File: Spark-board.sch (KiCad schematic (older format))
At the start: 12 parts

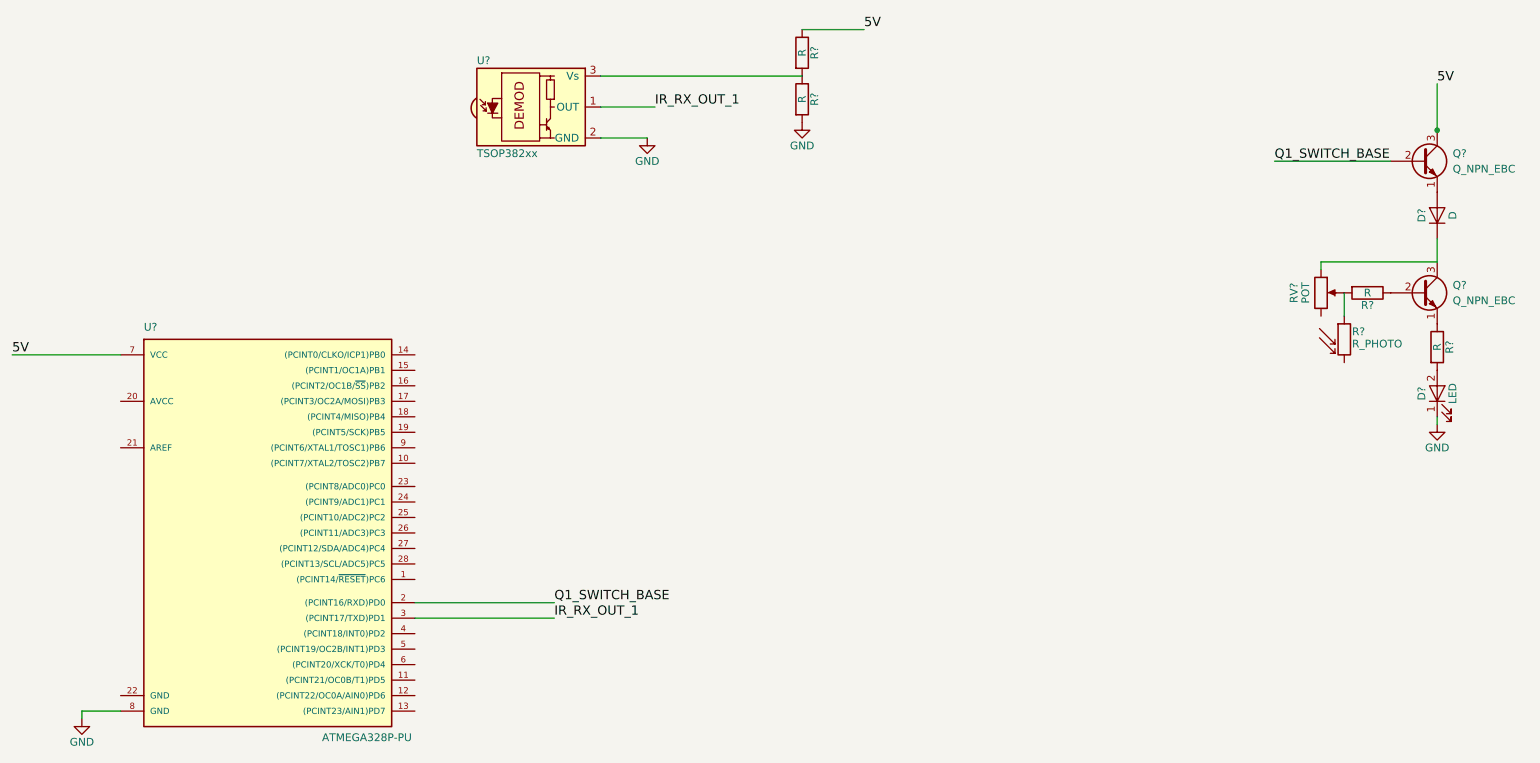
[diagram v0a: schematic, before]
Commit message: - Annotated components
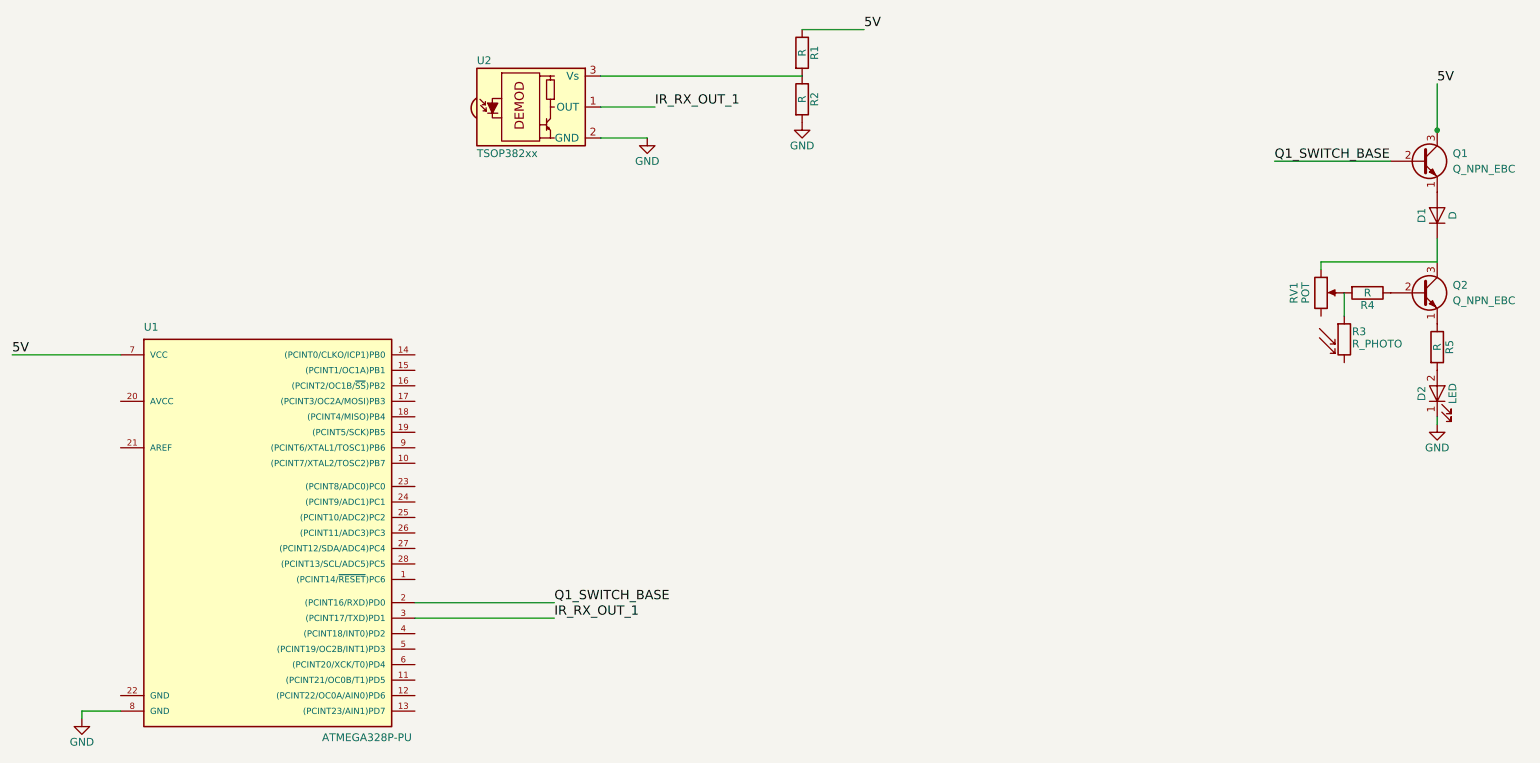
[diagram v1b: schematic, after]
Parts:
- gave numbers to parts that had none: 12
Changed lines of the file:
@@
 $EndDescr
 $Comp
-L POT RV?
+L POT RV1
 U 1 1 5BE8E67D
 P 9250 2400
-F 0 "RV?" V 9075 2400 50  0000 C CNN
+F 0 "RV1" V 9075 2400 50  0000 C CNN
 F 1 "POT" V 9150 2400 50  0000 C CNN
 F 2 "" H 9250 2400 50  0001 C CNN
@@
 $EndComp
 $Comp
-L D D?
+L D D1
 U 1 1 5BE8E73B
 P 10000 1900
-F 0 "D?" H 10000 2000 50  0000 C CNN
+F 0 "D1" H 10000 2000 50  0000 C CNN
 F 1 "D" H 10000 1800 50  0000 C CNN
 F 2 "" H 10000 1900 50  0001 C CNN
@@
 $EndComp
 $Comp
-L Q_NPN_EBC Q?
+L Q_NPN_EBC Q1
 U 1 1 5BE8E792
 P 9900 1550
-F 0 "Q?" H 10100 1600 50  0000 L CNN
+F 0 "Q1" H 10100 1600 50  0000 L CNN
 F 1 "Q_NPN_EBC" H 10100 1500 50  0000 L CNN
 F 2 "" H 10100 1650 50  0001 C CNN
@@
 $EndComp
 $Comp
-L Q_NPN_EBC Q?
+L Q_NPN_EBC Q2
 U 1 1 5BE8E8A3
 P 9900 2400
-F 0 "Q?" H 10100 2450 50  0000 L CNN
+F 0 "Q2" H 10100 2450 50  0000 L CNN
 F 1 "Q_NPN_EBC" H 10100 2350 50  0000 L CNN
 F 2 "" H 10100 2500 50  0001 C CNN
@@
 $EndComp
 $Comp
-L R R?
+L R R4
 U 1 1 5BE8EA00
 P 9550 2400
-F 0 "R?" V 9630 2400 50  0000 C CNN
+F 0 "R4" V 9630 2400 50  0000 C CNN
 F 1 "R" V 9550 2400 50  0000 C CNN
 F 2 "" V 9480 2400 50  0001 C CNN
@@
 	10000 2200 10000 2050
 $Comp
-L R R?
+L R R5
 U 1 1 5BE8EB2A
 P 10000 2750
-F 0 "R?" V 10080 2750 50  0000 C CNN
+F 0 "R5" V 10080 2750 50  0000 C CNN
 F 1 "R" V 10000 2750 50  0000 C CNN
 F 2 "" V 9930 2750 50  0001 C CNN
@@
 $EndComp
 $Comp
-L LED D?
+L LED D2
 U 1 1 5BE8EB6D
 P 10000 3050
-F 0 "D?" H 10000 3150 50  0000 C CNN
+F 0 "D2" H 10000 3150 50  0000 C CNN
 F 1 "LED" H 10000 2950 50  0000 C CNN
 F 2 "" H 10000 3050 50  0001 C CNN
@@
 $EndComp
 $Comp
-L GND #PWR?
+L GND #PWR4
 U 1 1 5BE8EDF4
 P 10000 3250
-F 0 "#PWR?" H 10000 3000 50  0001 C CNN
+F 0 "#PWR4" H 10000 3000 50  0001 C CNN
 F 1 "GND" H 10000 3100 50  0000 C CNN
 F 2 "" H 10000 3250 50  0001 C CNN
@@
 	10000 3200 10000 3250
 $Comp
-L R_PHOTO R?
+L R_PHOTO R3
 U 1 1 5BE8EE4E
 P 9400 2700
-F 0 "R?" H 9450 2750 50  0000 L CNN
+F 0 "R3" H 9450 2750 50  0000 L CNN
 F 1 "R_PHOTO" H 9450 2700 50  0000 L TNN
 F 2 "" V 9450 2450 50  0001 L CNN
@@
 	9400 2550 9400 2400
 $Comp
-L ATMEGA328P-PU U?
+L ATMEGA328P-PU U1
 U 1 1 5BE8F131
 P 2400 3900
-F 0 "U?" H 1650 5150 50  0000 L BNN
+F 0 "U1" H 1650 5150 50  0000 L BNN
 F 1 "ATMEGA328P-PU" H 2800 2500 50  0000 L BNN
 F 2 "DIL28" H 2400 3900 50  0001 C CIN
@@
 Connection ~ 10000 1350
 $Comp
-L GND #PWR?
+L GND #PWR1
 U 1 1 5BEA3ECB
 P 1250 5150
-F 0 "#PWR?" H 1250 4900 50  0001 C CNN
+F 0 "#PWR1" H 1250 4900 50  0001 C CNN
 F 1 "GND" H 1250 5000 50  0000 C CNN
 F 2 "" H 1250 5150 50  0001 C CNN
@@
 5V
 $Comp
-L TSOP382xx U?
+L TSOP382xx U2
 U 1 1 5BF22523
 P 4200 1200
-F 0 "U?" H 3800 1500 50  0000 L CNN
+F 0 "U2" H 3800 1500 50  0000 L CNN
 F 1 "TSOP382xx" H 3800 900 50  0000 L CNN
 F 2 "Opto-Devices:IRReceiver_Vishay_MINICAST-3pin" H 4150 825 50  0001 C CNN
@@
 $EndComp
 $Comp
-L GND #PWR?
+L GND #PWR2
 U 1 1 5BF225DA
 P 4900 1400
-F 0 "#PWR?" H 4900 1150 50  0001 C CNN
+F 0 "#PWR2" H 4900 1150 50  0001 C CNN
 F 1 "GND" H 4900 1250 50  0000 C CNN
 F 2 "" H 4900 1400 50  0001 C CNN
@@
 	4600 1400 4900 1400
 $Comp
-L R R?
+L R R2
 U 1 1 5BF22754
 P 5900 1150
-F 0 "R?" V 5980 1150 50  0000 C CNN
+F 0 "R2" V 5980 1150 50  0000 C CNN
 F 1 "R" V 5900 1150 50  0000 C CNN
 F 2 "" V 5830 1150 50  0001 C CNN
@@
 $EndComp
 $Comp
-L R R?
+L R R1
 U 1 1 5BF227B9
 P 5900 850
-F 0 "R?" V 5980 850 50  0000 C CNN
+F 0 "R1" V 5980 850 50  0000 C CNN
 F 1 "R" V 5900 850 50  0000 C CNN
 F 2 "" V 5830 850 50  0001 C CNN
@@
 5V
 $Comp
-L GND #PWR?
+L GND #PWR3
 U 1 1 5BF22B42
 P 5900 1300
-F 0 "#PWR?" H 5900 1050 50  0001 C CNN
+F 0 "#PWR3" H 5900 1050 50  0001 C CNN
 F 1 "GND" H 5900 1150 50  0000 C CNN
 F 2 "" H 5900 1300 50  0001 C CNN

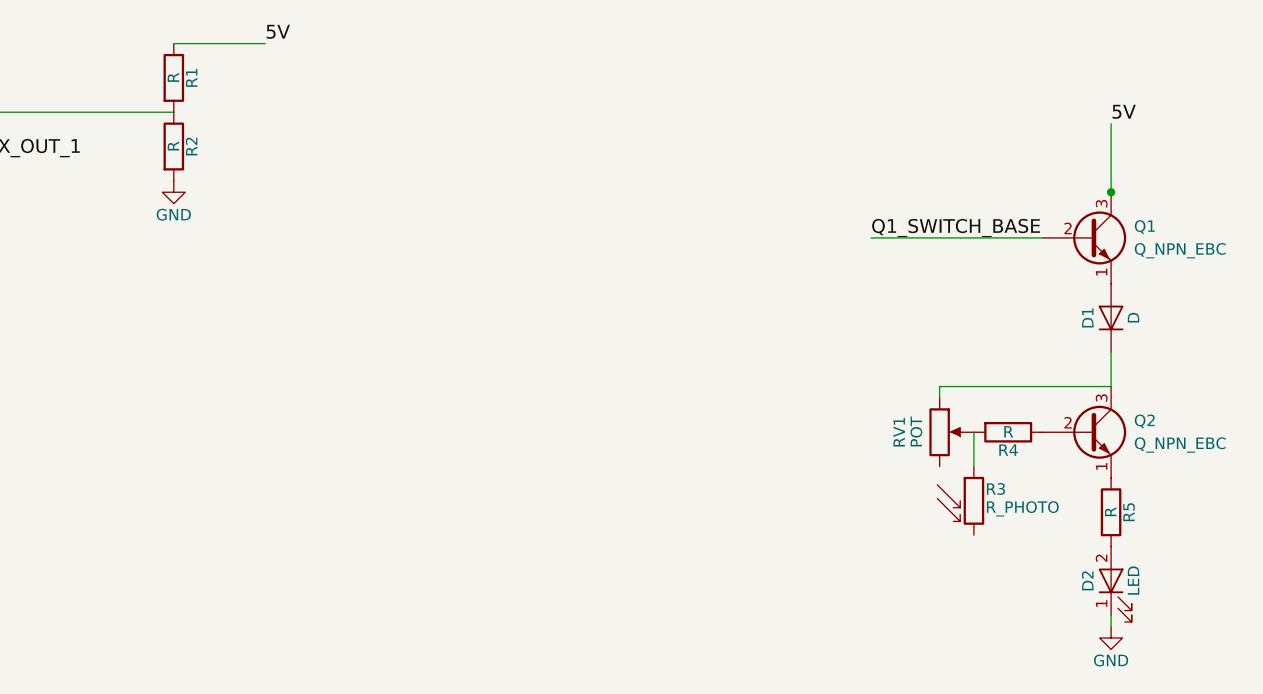
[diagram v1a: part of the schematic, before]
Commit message: - Added values to all resistors
- IR Rx receiver: Voltage divider should provide ~3.3V at Vs input
- Q1 Base: Voltage divider should provide adequate voltage to just keep LED off
           while ensure low current through transistor base
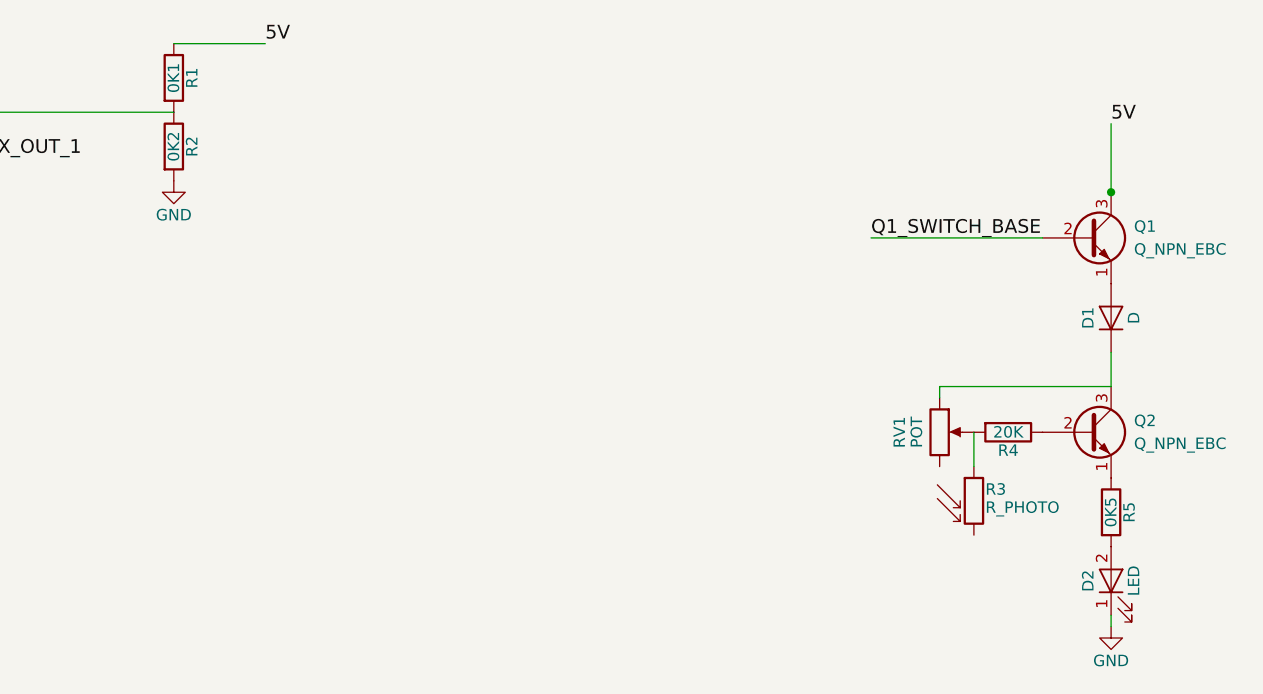
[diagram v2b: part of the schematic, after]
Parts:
- R1: value R -> 0K1
- R2: value R -> 0K2
- R4: value R -> 20K
- R5: value R -> 0K5
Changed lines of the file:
@@
 P 9550 2400
 F 0 "R4" V 9630 2400 50  0000 C CNN
-F 1 "R" V 9550 2400 50  0000 C CNN
+F 1 "20K" V 9550 2400 50  0000 C CNN
 F 2 "" V 9480 2400 50  0001 C CNN
 F 3 "" H 9550 2400 50  0001 C CNN
@@
 P 10000 2750
 F 0 "R5" V 10080 2750 50  0000 C CNN
-F 1 "R" V 10000 2750 50  0000 C CNN
+F 1 "0K5" V 10000 2750 50  0000 C CNN
 F 2 "" V 9930 2750 50  0001 C CNN
 F 3 "" H 10000 2750 50  0001 C CNN
@@
 P 5900 1150
 F 0 "R2" V 5980 1150 50  0000 C CNN
-F 1 "R" V 5900 1150 50  0000 C CNN
+F 1 "0K2" V 5900 1150 50  0000 C CNN
 F 2 "" V 5830 1150 50  0001 C CNN
 F 3 "" H 5900 1150 50  0001 C CNN
@@
 P 5900 850
 F 0 "R1" V 5980 850 50  0000 C CNN
-F 1 "R" V 5900 850 50  0000 C CNN
+F 1 "0K1" V 5900 850 50  0000 C CNN
 F 2 "" V 5830 850 50  0001 C CNN
 F 3 "" H 5900 850 50  0001 C CNN

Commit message: Imported new footprint libraries
PN2222, ATMEGA328P-PU, PDV-P8103
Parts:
- D1: footprint (none) -> Diodes_SMD:D_0603
- D2: footprint (none) -> LEDs:LED-L1T2_LUMILEDS
- Q1, Q2: footprint (none) -> PN2222:TO92
- R1, R2, R4, R5: footprint (none) -> Resistors_SMD:R_0603_HandSoldering
- R3: footprint (none) -> PDV-P8103:PHODET_PDV-P8103
- RV1: footprint (none) -> Potentiometers:Potentiometer_Alps_RK09K_Vertical
- U1: footprint DIL28 -> ATMEGA328P-PU:DIP254P762X457-28
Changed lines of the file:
@@
 LIBS:contrib
 LIBS:valves
+LIBS:ATMEGA328P-PU
+LIBS:PDV-P8103
+LIBS:PN2222
 LIBS:Spark-board-cache
 EELAYER 25 0
@@
 F 0 "RV1" V 9075 2400 50  0000 C CNN
 F 1 "POT" V 9150 2400 50  0000 C CNN
-F 2 "" H 9250 2400 50  0001 C CNN
+F 2 "Potentiometers:Potentiometer_Alps_RK09K_Vertical" H 9250 2400 50  0001 C CNN
 F 3 "" H 9250 2400 50  0001 C CNN
 	1    9250 2400
@@
 F 0 "D1" H 10000 2000 50  0000 C CNN
 F 1 "D" H 10000 1800 50  0000 C CNN
-F 2 "" H 10000 1900 50  0001 C CNN
+F 2 "Diodes_SMD:D_0603" H 10000 1900 50  0001 C CNN
 F 3 "" H 10000 1900 50  0001 C CNN
 	1    10000 1900
@@
 F 0 "Q1" H 10100 1600 50  0000 L CNN
 F 1 "Q_NPN_EBC" H 10100 1500 50  0000 L CNN
-F 2 "" H 10100 1650 50  0001 C CNN
+F 2 "PN2222:TO92" H 10100 1650 50  0001 C CNN
 F 3 "" H 9900 1550 50  0001 C CNN
 	1    9900 1550
@@
 F 0 "Q2" H 10100 2450 50  0000 L CNN
 F 1 "Q_NPN_EBC" H 10100 2350 50  0000 L CNN
-F 2 "" H 10100 2500 50  0001 C CNN
+F 2 "PN2222:TO92" H 10100 2500 50  0001 C CNN
 F 3 "" H 9900 2400 50  0001 C CNN
 	1    9900 2400
@@
 F 0 "R4" V 9630 2400 50  0000 C CNN
 F 1 "20K" V 9550 2400 50  0000 C CNN
-F 2 "" V 9480 2400 50  0001 C CNN
+F 2 "Resistors_SMD:R_0603_HandSoldering" V 9480 2400 50  0001 C CNN
 F 3 "" H 9550 2400 50  0001 C CNN
 	1    9550 2400
@@
 F 0 "R5" V 10080 2750 50  0000 C CNN
 F 1 "0K5" V 10000 2750 50  0000 C CNN
-F 2 "" V 9930 2750 50  0001 C CNN
+F 2 "Resistors_SMD:R_0603_HandSoldering" V 9930 2750 50  0001 C CNN
 F 3 "" H 10000 2750 50  0001 C CNN
 	1    10000 2750
@@
 F 0 "D2" H 10000 3150 50  0000 C CNN
 F 1 "LED" H 10000 2950 50  0000 C CNN
-F 2 "" H 10000 3050 50  0001 C CNN
+F 2 "LEDs:LED-L1T2_LUMILEDS" H 10000 3050 50  0001 C CNN
 F 3 "" H 10000 3050 50  0001 C CNN
 	1    10000 3050
@@
 $EndComp
 $Comp
-L GND #PWR4
+L GND #PWR01
 U 1 1 5BE8EDF4
 P 10000 3250
-F 0 "#PWR4" H 10000 3000 50  0001 C CNN
+F 0 "#PWR01" H 10000 3000 50  0001 C CNN
 F 1 "GND" H 10000 3100 50  0000 C CNN
 F 2 "" H 10000 3250 50  0001 C CNN
@@
 F 0 "R3" H 9450 2750 50  0000 L CNN
 F 1 "R_PHOTO" H 9450 2700 50  0000 L TNN
-F 2 "" V 9450 2450 50  0001 L CNN
+F 2 "PDV-P8103:PHODET_PDV-P8103" V 9450 2450 50  0001 L CNN
 F 3 "" H 9400 2650 50  0001 C CNN
 	1    9400 2700
@@
 F 0 "U1" H 1650 5150 50  0000 L BNN
 F 1 "ATMEGA328P-PU" H 2800 2500 50  0000 L BNN
-F 2 "DIL28" H 2400 3900 50  0001 C CIN
+F 2 "ATMEGA328P-PU:DIP254P762X457-28" H 2400 3900 50  0001 C CIN
 F 3 "" H 2400 3900 50  0001 C CNN
 	1    2400 3900
@@
 Connection ~ 10000 1350
 $Comp
-L GND #PWR1
+L GND #PWR02
 U 1 1 5BEA3ECB
 P 1250 5150
-F 0 "#PWR1" H 1250 4900 50  0001 C CNN
+F 0 "#PWR02" H 1250 4900 50  0001 C CNN
 F 1 "GND" H 1250 5000 50  0000 C CNN
 F 2 "" H 1250 5150 50  0001 C CNN
@@
 $EndComp
 $Comp
-L GND #PWR2
+L GND #PWR03
 U 1 1 5BF225DA
 P 4900 1400
-F 0 "#PWR2" H 4900 1150 50  0001 C CNN
+F 0 "#PWR03" H 4900 1150 50  0001 C CNN
 F 1 "GND" H 4900 1250 50  0000 C CNN
 F 2 "" H 4900 1400 50  0001 C CNN
@@
 F 0 "R2" V 5980 1150 50  0000 C CNN
 F 1 "0K2" V 5900 1150 50  0000 C CNN
-F 2 "" V 5830 1150 50  0001 C CNN
+F 2 "Resistors_SMD:R_0603_HandSoldering" V 5830 1150 50  0001 C CNN
 F 3 "" H 5900 1150 50  0001 C CNN
 	1    5900 1150
@@
 F 0 "R1" V 5980 850 50  0000 C CNN
 F 1 "0K1" V 5900 850 50  0000 C CNN
-F 2 "" V 5830 850 50  0001 C CNN
+F 2 "Resistors_SMD:R_0603_HandSoldering" V 5830 850 50  0001 C CNN
 F 3 "" H 5900 850 50  0001 C CNN
 	1    5900 850
@@
 5V
 $Comp
-L GND #PWR3
+L GND #PWR04
 U 1 1 5BF22B42
 P 5900 1300
-F 0 "#PWR3" H 5900 1050 50  0001 C CNN
+F 0 "#PWR04" H 5900 1050 50  0001 C CNN
 F 1 "GND" H 5900 1150 50  0000 C CNN
 F 2 "" H 5900 1300 50  0001 C CNN

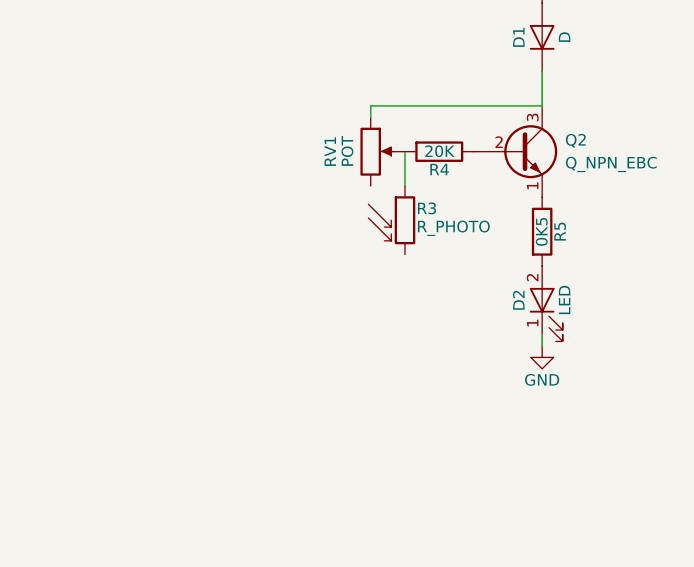
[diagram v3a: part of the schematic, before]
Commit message: Added ground to one photo-resistor on schematic and re-generated netlist
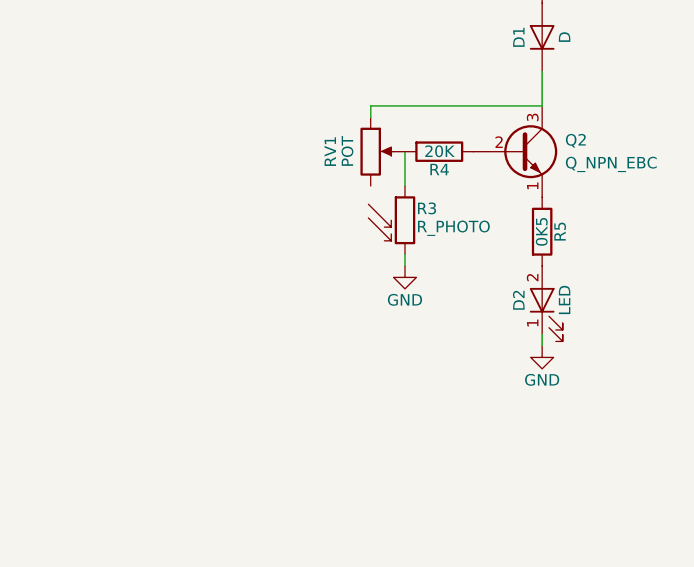
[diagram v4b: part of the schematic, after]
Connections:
- net GND: now also R3.2
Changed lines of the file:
@@
 Text Label 4300 4500 0    60   ~ 0
 IR_RX_OUT_1
+$Comp
+L GND #PWR05
+U 1 1 5C060178
+P 9400 2900
+F 0 "#PWR05" H 9400 2650 50  0001 C CNN
+F 1 "GND" H 9400 2750 50  0000 C CNN
+F 2 "" H 9400 2900 50  0001 C CNN
+F 3 "" H 9400 2900 50  0001 C CNN
+	1    9400 2900
+	1    0    0    -1
+$EndComp
+Wire Wire Line
+	9400 2850 9400 2900
 $EndSCHEMATC
